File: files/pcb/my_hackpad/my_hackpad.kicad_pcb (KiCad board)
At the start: 2 copper layers, 32 parts, among them SW1 CherryMX, SW10 CherryMX, SW11 CherryMX, SW12 CherryMX, SW13 CherryMX, SW14 CherryMX, SW15 CherryMX, SW16 RotaryEncoder_Switch, SW2 CherryMX, SW3 CherryMX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

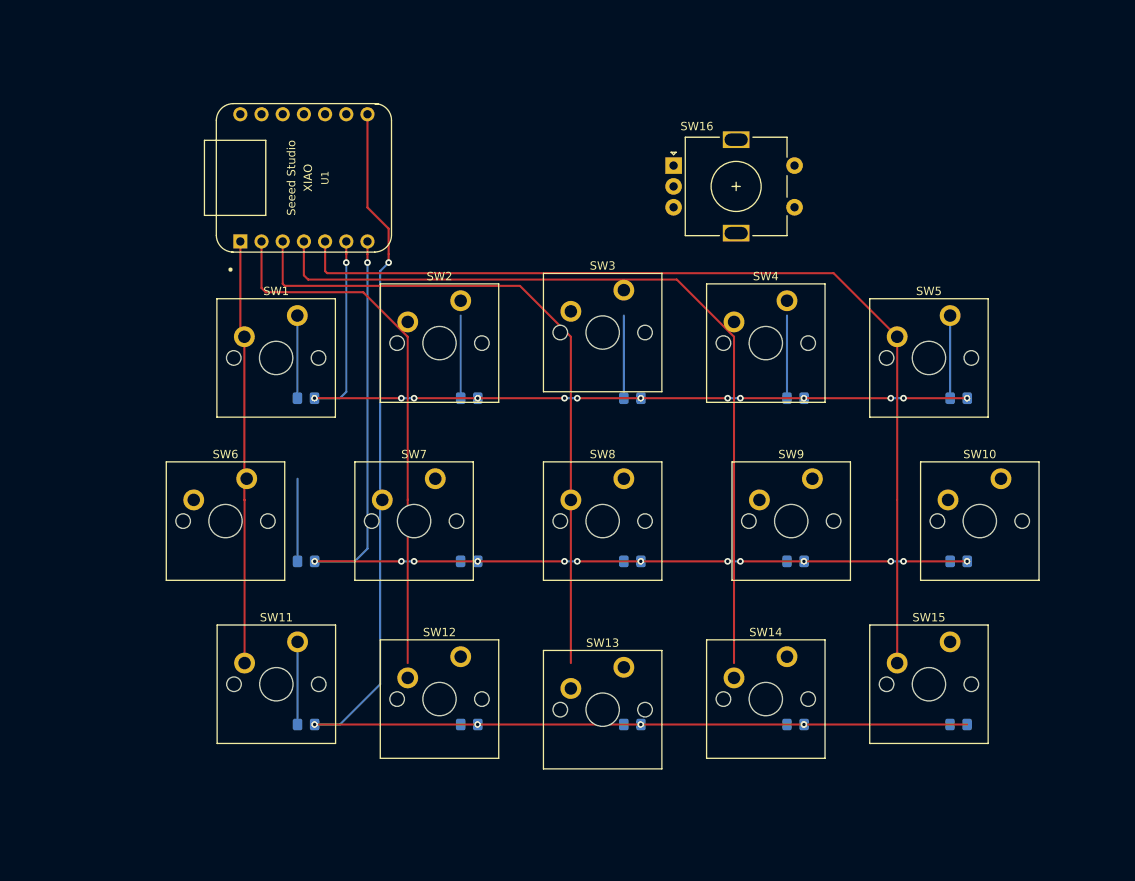
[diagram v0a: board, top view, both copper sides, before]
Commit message: Libraries added, case design started, PCB routing complete
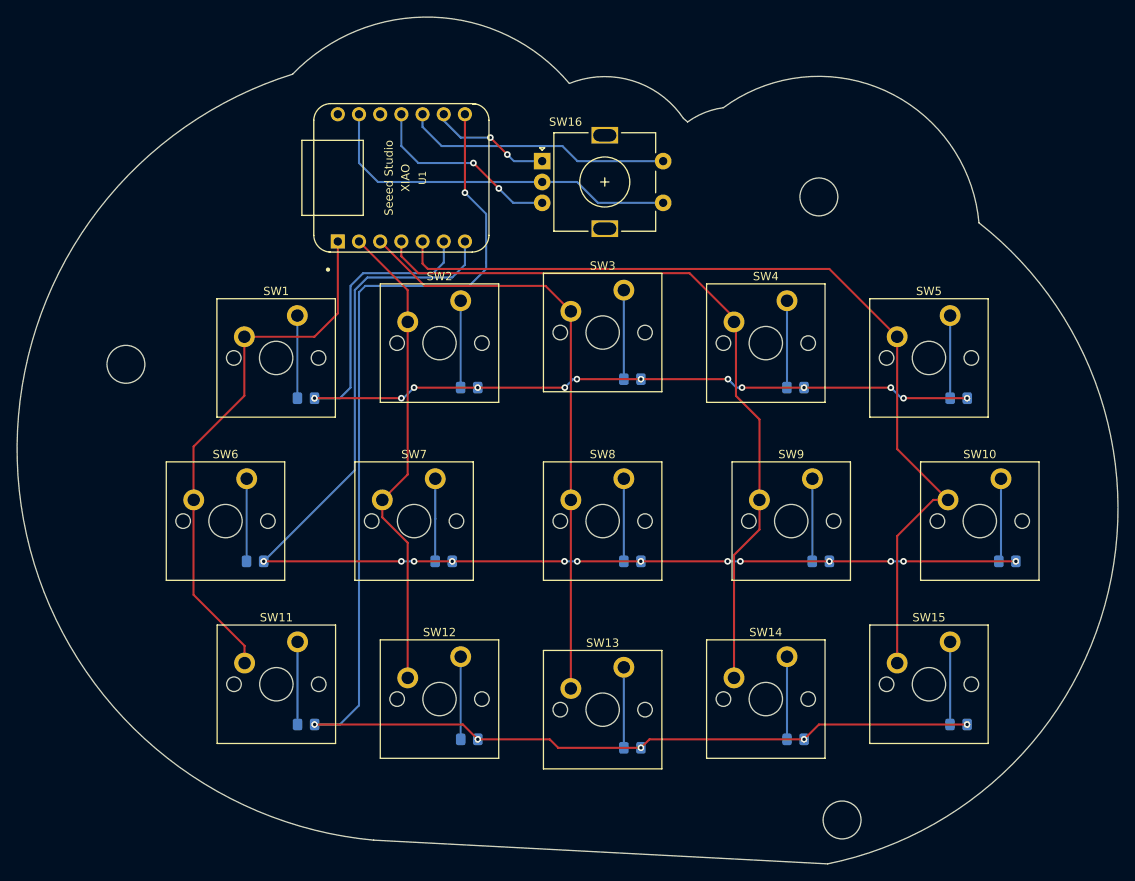
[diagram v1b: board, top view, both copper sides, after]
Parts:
- moved SW16 15.8 mm to (127.1, 56.7)
- moved U1 11.7 mm to (110.2, 58.7)
- moved D6 6.11 mm to (92.7, 104.6)
- moved D10 5.83 mm to (182.9, 104.6)
- moved D7 3.05 mm to (115.3, 104.6)
- moved D9 3.03 mm to (160.5, 104.6)
- moved D13 2.79 mm to (137.9, 127.0)
- moved D3 2.29 mm to (137.9, 82.8)
- moved D12 1.78 mm to (118.4, 126.0)
- moved D14 1.78 mm to (157.5, 126.0)
- moved D4 1.27 mm to (157.5, 83.8)
- moved D2 1.27 mm to (118.4, 83.8)
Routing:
- net GND: track 0.00 -> 44.3 mm
- net EC11SW: track 0.00 -> 32.1 mm
- net EC11B: track 0.00 -> 23.5 mm, vias 0 -> 2
- net ROW1: track 122.0 -> 144.5 mm, vias 14 -> 13
- net COL0: track 50.8 -> 65.8 mm
- net EC11A: track 0.00 -> 14.6 mm, vias 0 -> 2
- net ROW2: track 157.9 -> 172.3 mm, vias 5 -> 6
- net ROW0: track 100.6 -> 112.0 mm, vias 14 -> 13
- net Net-(D10-A): track 0.00 -> 10.0 mm
- net Net-(D15-A): track 0.00 -> 9.91 mm
- net Net-(D9-A): track 0.00 -> 9.91 mm
- net Net-(D7-A): track 0.00 -> 9.91 mm
- net Net-(D8-A): track 0.00 -> 9.91 mm
- net Net-(D14-A): track 0.00 -> 9.91 mm
- net Net-(D12-A): track 0.00 -> 9.91 mm
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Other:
- board outline added: 132 x 101.5 mm

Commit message: PCB Finished
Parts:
- moved U1 11.5 mm to (98.8, 58.3)
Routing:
- net COL2: track 71.5 -> 84.4 mm
- net ROW2: track 172.3 -> 159.9 mm
- net EC11SW: track 32.1 -> 44.3 mm
- net EC11A: track 14.6 -> 26.9 mm
- net GND: track 44.3 -> 56.5 mm
- net EC11B: track 23.5 -> 35.5 mm
- net COL3: track 89.9 -> 101.4 mm
- net COL1: track 57.3 -> 68.2 mm
- net COL4: track 108.4 -> 119.3 mm
- net ROW1: track 144.5 -> 134.1 mm
- net COL0: track 65.8 -> 56.8 mm
- net ROW0: track 112.0 -> 103.0 mm
